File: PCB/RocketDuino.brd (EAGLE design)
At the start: 73 x 41 mm, 41 parts, among them J1 FTDI, Y1 16MHZ

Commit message: Very minor board movements
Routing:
- net GND: vias 20 -> 21
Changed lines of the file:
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@@
 <wire x1="45.75" y1="13.75" x2="45.85" y2="13.65" width="1.016" layer="1"/>
 <wire x1="45.85" y1="13.65" x2="48" y2="13.65" width="1.016" layer="1"/>
+<polygon width="0.254" layer="1" isolate="1" thermals="no" rank="4">
+<vertex x="62" y="20"/>
+<vertex x="63" y="20" curve="-90"/>
+<vertex x="67" y="16"/>
+<vertex x="67" y="15" curve="90"/>
+<vertex x="68" y="14" curve="90"/>
+<vertex x="69" y="15"/>
+<vertex x="69" y="17" curve="90"/>
+<vertex x="63" y="22"/>
+<vertex x="62" y="22"/>
+</polygon>
+<via x="66" y="19" extent="1-16" drill="0.6"/>
 </signal>
 <signal name="RESET">

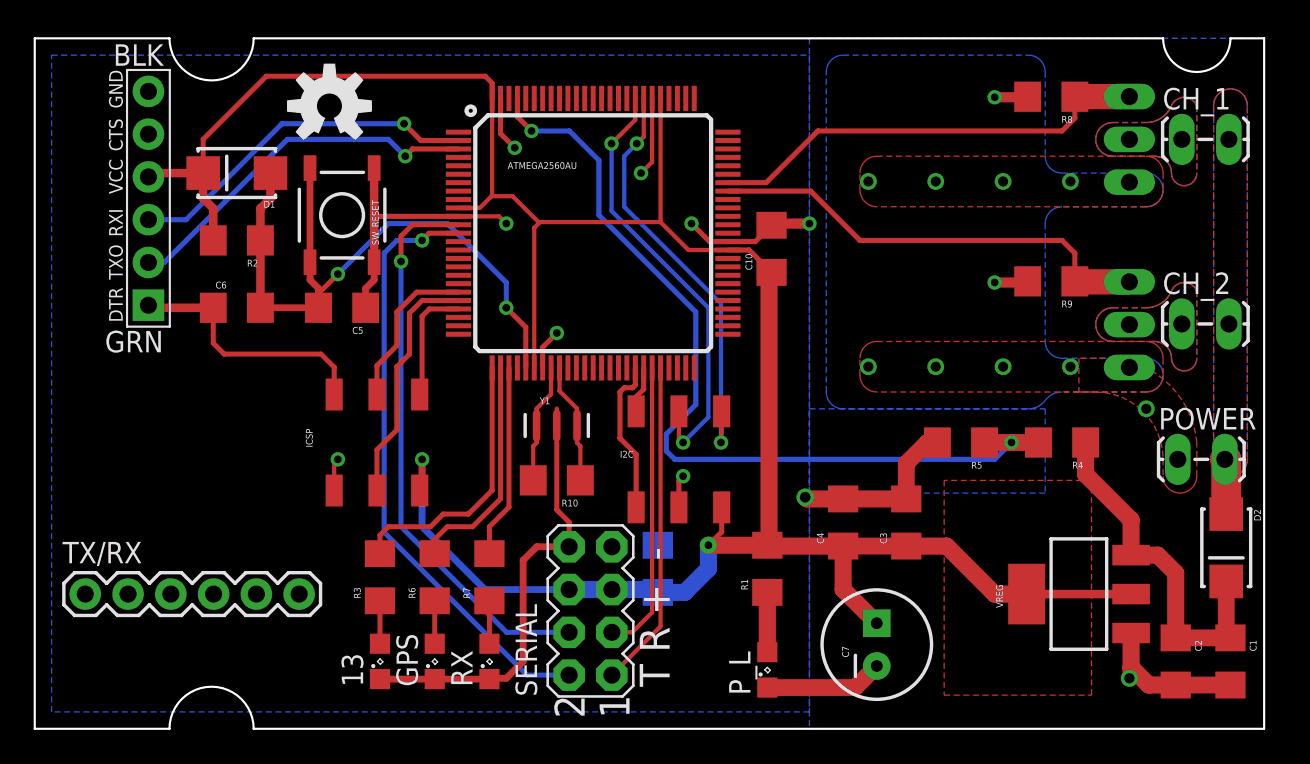
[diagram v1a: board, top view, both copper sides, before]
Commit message: Clean schematic; Shift Board componets
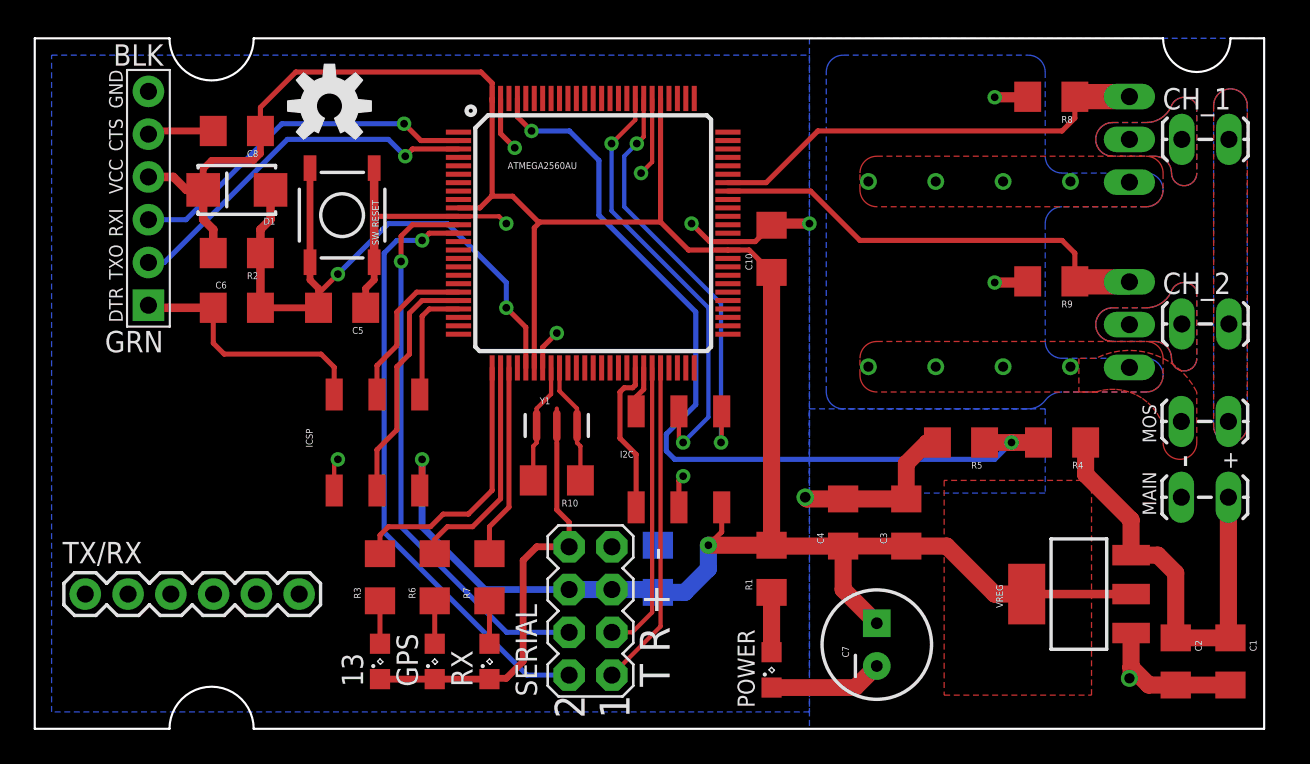
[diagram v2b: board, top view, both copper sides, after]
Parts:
- removed D2: (no value), SparkFun-DiscreteSemi:SMA-DIODE_ALT
- removed P_L: (no value), led:SML0805
- added C8: 10uF, SparkFun-Capacitors:1206
- added MAIN, MOS: (no value), SparkFun-Connectors:1X02_LOCK_LONGPADS
- POWER: device SparkFun-Connectors:1X02_LOCK_LONGPADS -> led:SML0805
- moved POWER 27.3 mm to (43.8, 3.50), turned to 90 degrees
- moved D1 1.00 mm to (12.0, 32.0)
- moved R2 0.75 mm to (12.0, 28.2)
- moved R1 0.25 mm to (43.8, 9.50)
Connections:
- removed net VIN_RECTIFIED: C1.1, C2.1, D2.C, R4.1, VREG.3
- new net VIN_MOS: CH_1.2, CH_2.2, MOS.1
- net 5V: now also C8.1
- net GND: now also C8.2, MAIN.2, MOS.2, POWER.C; no longer POWER.1, P_L.C
- net N$2: now also POWER.A; no longer P_L.A
- net VIN: now also C1.1, C2.1, MAIN.1, R4.1, VREG.3; no longer CH_1.2, CH_2.2, D2.A, POWER.2
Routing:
- net VIN: track 3.33 -> 26.8 mm
- net VIN_RECTIFIED: track 21.5 -> 0.00 mm
- net GND: track 94.2 -> 97.9 mm, vias 21 -> 20
- net 5V: track 149.5 -> 152.0 mm
- net RESET: track 41.3 -> 39.9 mm
- added copper zone on layer 1, net VIN_MOS
- added copper zone on layer 16, net VIN_MOS
- removed copper zone on layer 1, net VIN
- removed copper zone on layer 16, net VIN
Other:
- board text added: "+"
- board text added: "-"

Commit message: tired
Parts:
- removed TX/RX: (no value), SparkFun-Connectors:1X06
- moved ICSP 7.27 mm to (13.1, 17.5)
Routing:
- net DTR: track 15.4 -> 8.59 mm
- net SCK: track 9.54 -> 15.4 mm
- net MOSI: track 14.6 -> 20.0 mm
- net MISO: track 7.05 -> 12.2 mm
- net 5V: track 152.0 -> 155.7 mm
- net GND: track 97.9 -> 98.5 mm
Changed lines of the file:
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@@
 <element name="R4" library="SparkFun-Resistors" package="1206" value="470KΩ" x="61" y="17" rot="R180"/>
 <element name="R5" library="SparkFun-Resistors" package="1206" value="100KΩ" x="55" y="17" rot="R180"/>
-<element name="ICSP" library="SparkFun-Connectors" package="2X3_SMD" value="" x="20.32" y="17" smashed="yes" rot="R180">
-<attribute name="PROD_ID" value="CONN-11290" x="20.32" y="17" size="1.778" layer="27" rot="R180" display="off"/>
-<attribute name="NAME" x="16.1" y="17.822" size="0.4064" layer="25" rot="R270"/>
-<attribute name="VALUE" x="23.822" y="17.408" size="0.4064" layer="27" rot="R180"/>
+<element name="ICSP" library="SparkFun-Connectors" package="2X3_SMD" value="" x="13.07" y="17.5" smashed="yes" rot="R180">
+<attribute name="PROD_ID" value="CONN-11290" x="13.07" y="17.5" size="1.778" layer="27" rot="R180" display="off"/>
+<attribute name="NAME" x="8.85" y="18.322" size="0.4064" layer="25" rot="R270"/>
+<attribute name="VALUE" x="16.572" y="17.908" size="0.4064" layer="27" rot="R180"/>
 </element>
 <element name="POWER" library="led" package="SML0805" value="" x="43.75" y="3.5" smashed="yes" rot="R90">
@@
 <element name="I2C" library="SparkFun-Connectors" package="2X3_SMD" value="" x="38.25" y="16">
 <attribute name="PROD_ID" value="CONN-11290" x="38.25" y="16" size="1.778" layer="27" display="off"/>
-</element>
-<element name="TX/RX" library="SparkFun-Connectors" package="1X06" value="" x="3" y="8">
-<attribute name="PROD_ID" value="CONN-08437" x="3" y="8" size="1.778" layer="27" display="off"/>
 </element>
 <element name="FRAME1" library="SparkFun-Aesthetics" package="CREATIVE_COMMONS" value="FRAME-LEDGER" x="21" y="-8"/>
@@
 <via x="28" y="30" extent="1-16" drill="0.4572"/>
 <via x="31" y="23.5" extent="1-16" drill="0.4572"/>
-<wire x1="17.78" y1="14.15" x2="17.78" y2="15.78" width="0.254" layer="1"/>
-<wire x1="17.78" y1="15.78" x2="18" y2="16" width="0.254" layer="1"/>
-<via x="18" y="16" extent="1-16" drill="0.4572"/>
 <polygon width="0.254" layer="16" isolate="0.5">
 <vertex x="1" y="40"/>
@@
 <wire x1="6.75" y1="35.31" x2="6.94" y2="35.5" width="0.4064" layer="1"/>
 <wire x1="6.94" y1="35.5" x2="10.6" y2="35.5" width="0.4064" layer="1"/>
+<via x="11" y="17" extent="1-16" drill="0.4572"/>
+<wire x1="10.53" y1="14.65" x2="10.53" y2="16.53" width="0.3" layer="1"/>
+<wire x1="10.53" y1="16.53" x2="11" y2="17" width="0.3" layer="1"/>
 </signal>
 <signal name="RESET">
@@
 <signal name="DTR">
 <contactref element="J1" pad="P$1"/>
-<contactref element="C6" pad="1"/>
 <contactref element="ICSP" pad="5"/>
 <wire x1="6.75" y1="25.15" x2="6.9" y2="25" width="0.508" layer="1"/>
+<contactref element="C6" pad="1"/>
 <wire x1="6.9" y1="25" x2="10.6" y2="25" width="0.508" layer="1"/>
-<wire x1="17.78" y1="19.85" x2="17.78" y2="21.47" width="0.3" layer="1"/>
-<wire x1="17" y1="22.25" x2="11.25" y2="22.25" width="0.3" layer="1"/>
-<wire x1="10.6" y1="22.9" x2="10.6" y2="25" width="0.3" layer="1"/>
-<wire x1="10.6" y1="22.9" x2="11.25" y2="22.25" width="0.3" layer="1"/>
-<wire x1="17.78" y1="21.47" x2="17" y2="22.25" width="0.3" layer="1"/>
+<wire x1="10.53" y1="20.35" x2="10.53" y2="24.93" width="0.4064" layer="1"/>
+<wire x1="10.53" y1="24.93" x2="10.6" y2="25" width="0.4064" layer="1"/>
 </signal>
 <signal name="LED_13">
@@
 <wire x1="40" y1="10.9" x2="43.75" y2="10.9" width="1.016" layer="1"/>
 <wire x1="34.27" y1="8.27" x2="31.73" y2="8.27" width="1.016" layer="16"/>
-<wire x1="23" y1="12" x2="23" y2="16" width="0.4064" layer="16"/>
-<via x="23" y="16" extent="1-16" drill="0.4572"/>
-<wire x1="23" y1="16" x2="23" y2="14.29" width="0.4064" layer="1"/>
-<wire x1="23" y1="14.29" x2="22.86" y2="14.15" width="0.4064" layer="1"/>
+<wire x1="23" y1="12" x2="23" y2="14" width="0.4064" layer="16"/>
+<via x="23" y="14" extent="1-16" drill="0.4572"/>
 <wire x1="27.16" y1="31.66" x2="27.16" y2="37.43" width="0.3048" layer="1"/>
 <contactref element="I2C" pad="5"/>
@@
 <wire x1="13.4" y1="35.5" x2="13.4" y2="36.9" width="0.3048" layer="1"/>
 <wire x1="13.4" y1="36.9" x2="15.5" y2="39" width="0.3048" layer="1"/>
+<wire x1="23" y1="14" x2="22.35" y2="14.65" width="0.4064" layer="1"/>
+<wire x1="22.35" y1="14.65" x2="15.61" y2="14.65" width="0.4064" layer="1"/>
 </signal>
 <signal name="TX1">
@@
 <contactref element="ICSP" pad="3"/>
 <contactref element="ATMEGA2560AU" pad="20"/>
-<wire x1="25.16" y1="25.93" x2="22.68" y2="25.93" width="0.3" layer="1"/>
-<wire x1="21.5" y1="22.75" x2="20.32" y2="21.57" width="0.3" layer="1"/>
-<wire x1="20.32" y1="21.57" x2="20.32" y2="19.85" width="0.3" layer="1"/>
-<wire x1="21.5" y1="22.75" x2="21.5" y2="24.75" width="0.3" layer="1"/>
-<wire x1="21.5" y1="24.75" x2="22.68" y2="25.93" width="0.3" layer="1"/>
+<wire x1="25.16" y1="25.93" x2="23.43" y2="25.93" width="0.3" layer="1"/>
+<wire x1="20.5" y1="23" x2="14" y2="23" width="0.3" layer="1"/>
+<wire x1="14" y1="23" x2="13.07" y2="22.07" width="0.3" layer="1"/>
+<wire x1="13.07" y1="22.07" x2="13.07" y2="20.35" width="0.3" layer="1"/>
+<wire x1="23.43" y1="25.93" x2="20.5" y2="23" width="0.3" layer="1"/>
 </signal>
 <signal name="MISO">
 <contactref element="ICSP" pad="1"/>
 <contactref element="ATMEGA2560AU" pad="22"/>
-<wire x1="25.16" y1="24.93" x2="23.43" y2="24.93" width="0.3" layer="1"/>
-<wire x1="23.43" y1="24.93" x2="23" y2="24.5" width="0.3" layer="1"/>
-<wire x1="23" y1="24.5" x2="23" y2="19.99" width="0.3" layer="1"/>
-<wire x1="23" y1="19.99" x2="22.86" y2="19.85" width="0.3" layer="1"/>
+<wire x1="25.16" y1="24.93" x2="23.93" y2="24.93" width="0.3" layer="1"/>
+<wire x1="21" y1="22" x2="16" y2="22" width="0.3" layer="1"/>
+<wire x1="16" y1="22" x2="15.61" y2="21.61" width="0.3" layer="1"/>
+<wire x1="15.61" y1="21.61" x2="15.61" y2="20.35" width="0.3" layer="1"/>
+<wire x1="23.93" y1="24.93" x2="21" y2="22" width="0.3" layer="1"/>
 </signal>
 <signal name="MOSI">
 <contactref element="ICSP" pad="4"/>
 <contactref element="ATMEGA2560AU" pad="21"/>
-<wire x1="25.16" y1="25.43" x2="23" y2="25.43" width="0.3" layer="1"/>
-<wire x1="21.5" y1="17.75" x2="20.32" y2="16.57" width="0.3" layer="1"/>
-<wire x1="20.32" y1="16.57" x2="20.32" y2="14.15" width="0.3" layer="1"/>
-<wire x1="22.25" y1="22.25" x2="21.5" y2="21.5" width="0.3" layer="1"/>
-<wire x1="22.25" y1="22.25" x2="22.25" y2="24.68" width="0.3" layer="1"/>
-<wire x1="22.25" y1="24.68" x2="23" y2="25.43" width="0.3" layer="1"/>
-<wire x1="21.5" y1="21.5" x2="21.5" y2="17.75" width="0.3" layer="1"/>
+<wire x1="25.16" y1="25.43" x2="23.68" y2="25.43" width="0.3" layer="1"/>
+<wire x1="20.75" y1="22.5" x2="15" y2="22.5" width="0.3" layer="1"/>
+<wire x1="23.68" y1="25.43" x2="20.75" y2="22.5" width="0.3" layer="1"/>
+<wire x1="13.07" y1="14.65" x2="13.07" y2="16.07" width="0.3" layer="1"/>
+<wire x1="13.07" y1="16.07" x2="14.25" y2="17.25" width="0.3" layer="1"/>
+<wire x1="14.25" y1="17.25" x2="14.25" y2="21.75" width="0.3" layer="1"/>
+<wire x1="14.25" y1="21.75" x2="15" y2="22.5" width="0.3" layer="1"/>
 </signal>
 <signal name="N$2">

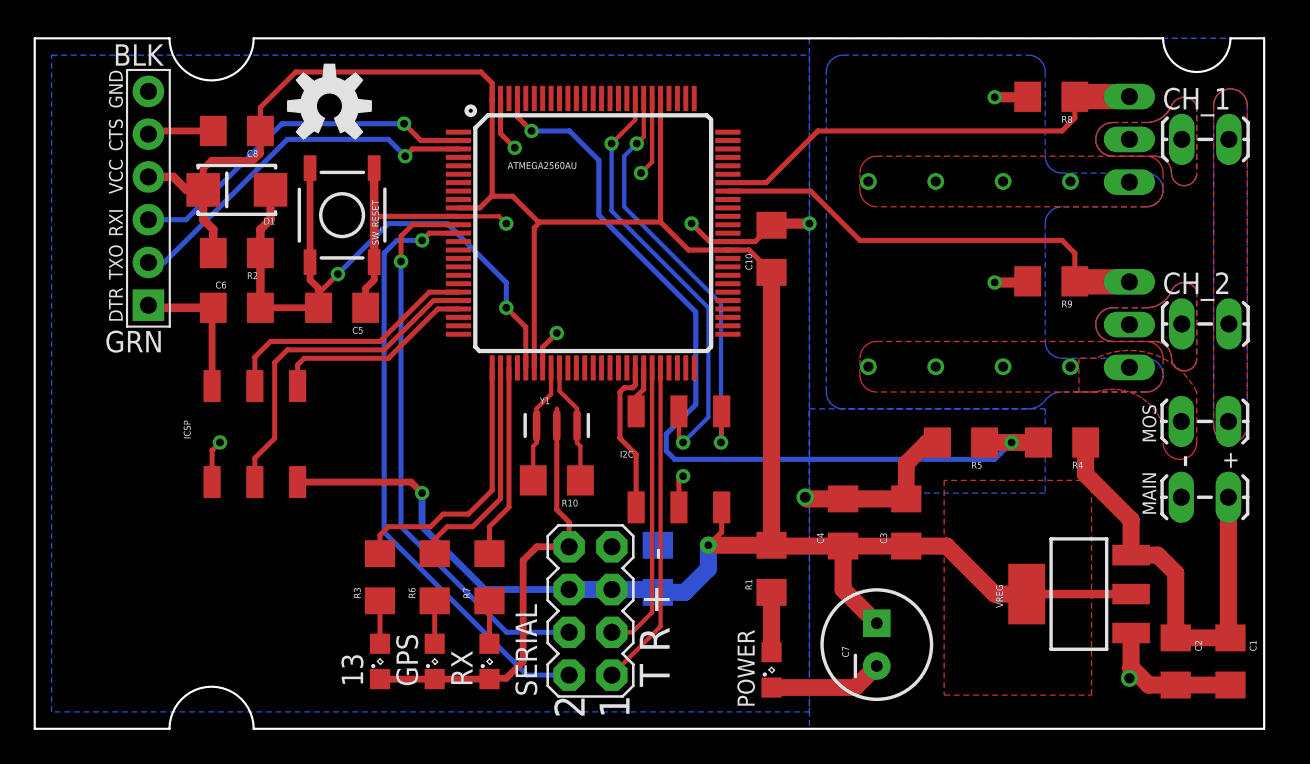
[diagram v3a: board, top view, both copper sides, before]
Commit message: Clean up all Silkscreen Indicators
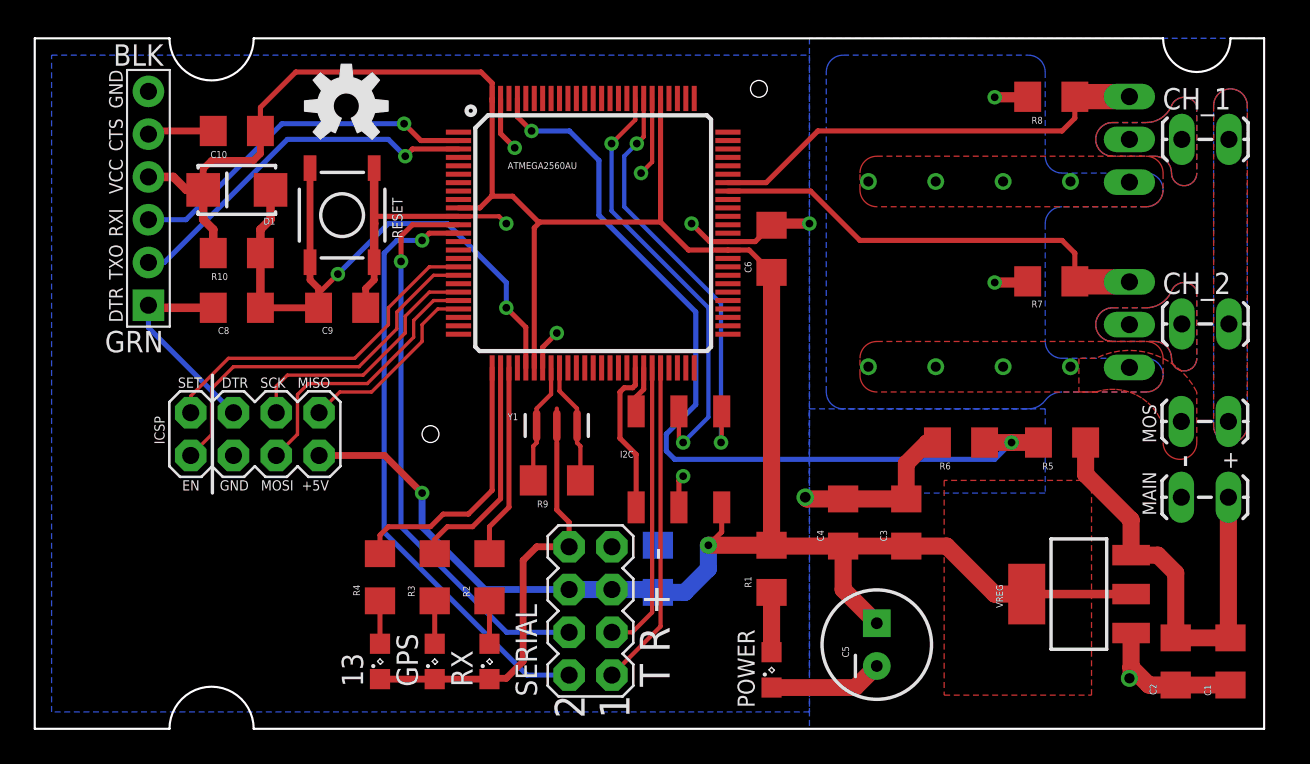
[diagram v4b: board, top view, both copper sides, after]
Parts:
- C10: value 0.1uF -> 10uF
- C5: value 0.22uF -> 470uF; device SparkFun-Capacitors:1206 -> SparkFun-Capacitors:CPOL-RADIAL-100UF-25V
- C7: value 470uF -> 10uF; device SparkFun-Capacitors:CPOL-RADIAL-100UF-25V -> SparkFun-Capacitors:1206
- C8: value 10uF -> 0.1uF
- C9: value 10uF -> 0.22uF
- ICSP: device SparkFun-Connectors:2X3_SMD -> SparkFun-Connectors:2X4
- R10: value 1MΩ -> 10KΩ
- R2: value 10KΩ -> 150Ω
- R3: value 150Ω -> 100Ω
- R4: value 470KΩ -> 150Ω
- R5: value 100KΩ -> 470KΩ
- R6: value 100Ω -> 100KΩ
- R7: value 150Ω -> 10KΩ
- R9: value 10KΩ -> 1MΩ
- moved R4 41.3 mm to (20.5, 9.00), turned to 90 degrees
- moved R7 37.7 mm to (60.4, 26.6), turned to 180 degrees
- moved C5 37.5 mm to (50.0, 5.00), turned to 90 degrees
- moved C10 32.5 mm to (12.0, 35.5), turned to 180 degrees
- moved R6 32.3 mm to (55.0, 17.0), turned to 180 degrees
- moved C6 31.9 mm to (43.8, 28.5), turned to 90 degrees
- moved R9 31.6 mm to (31.0, 14.8)
- moved R2 24.4 mm to (27.0, 9.00), turned to 90 degrees
- moved C9 24.3 mm to (18.2, 25.0), flipped to the top, turned to 180 degrees
- moved R10 23.3 mm to (12.0, 28.2)
- moved C7 13.8 mm to (37.0, 9.50), flipped to the bottom
- moved C8 10.5 mm to (12.0, 25.0), turned to 0 degrees
- moved R5 6.00 mm to (61.0, 17.0)
- moved R3 3.25 mm to (23.8, 9.00)
- moved LOGO1 1.00 mm to (18.5, 37.0)
- renumbered SW_RESET to RESET
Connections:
- new net EN: ATMEGA2560AU.18, ICSP.8
- new net SET: ATMEGA2560AU.17, ICSP.7
- net 5V: now also C5.1, C6.1, R10.2; no longer C8.1, C9.1, R2.2
- net CHARGE2: now also R7.1; no longer R9.1
- net DTR: now also C8.1; no longer C6.1
- net GND: now also C5.2, C6.2, C9.1, R6.2, R7.2; no longer C5.1, C8.2, C9.2, R5.2, R9.2
- net LED_13: now also R4.2; no longer R3.2
- net LED_GPS: now also R3.2; no longer R6.2
- net LED_RX: now also R2.2; no longer R7.2
- net N$1: now also R3.1; no longer R6.1
- net N$3: now also R4.1; no longer R3.1
- net N$4: now also R2.1; no longer R7.1
- net RESET: now also C8.2, C9.2, R10.1; no longer C5.2, C6.2, R2.1
- net VIN: now also R5.1; no longer R4.1
- net VSENSE: now also R5.2, R6.1; no longer R4.2, R5.1
- net XTAL1: now also R9.1; no longer R10.1
- net XTAL2: now also R9.2; no longer R10.2
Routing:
- net EN: track 0.00 -> 22.5 mm
- net SET: track 0.00 -> 20.7 mm
- net DTR: track 8.59 -> 12.5 mm
- net MOSI: track 20.0 -> 16.6 mm
- net GND: track 98.5 -> 96.0 mm, vias 20 -> 19
- net MISO: track 12.2 -> 11.4 mm
- net 5V: track 155.7 -> 155.1 mm
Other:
- board text added: "EN GND MOSI +5V"
- board text added: "SET DTR SCK MISO"
